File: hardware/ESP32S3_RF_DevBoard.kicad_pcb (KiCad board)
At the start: 4 copper layers, 25.4 x 60 mm, 35 parts, among them J1 USB4105-GF-A, J2 Conn_01x22, J3 Conn_01x22, SW1 BOOT, SW2 RESET, U1 ESD122DMYR, U2 LD1117DT33CTR, U3 ESP32-S3-WROOM-1-N8, U4 SN74AHCT1G125DBVR

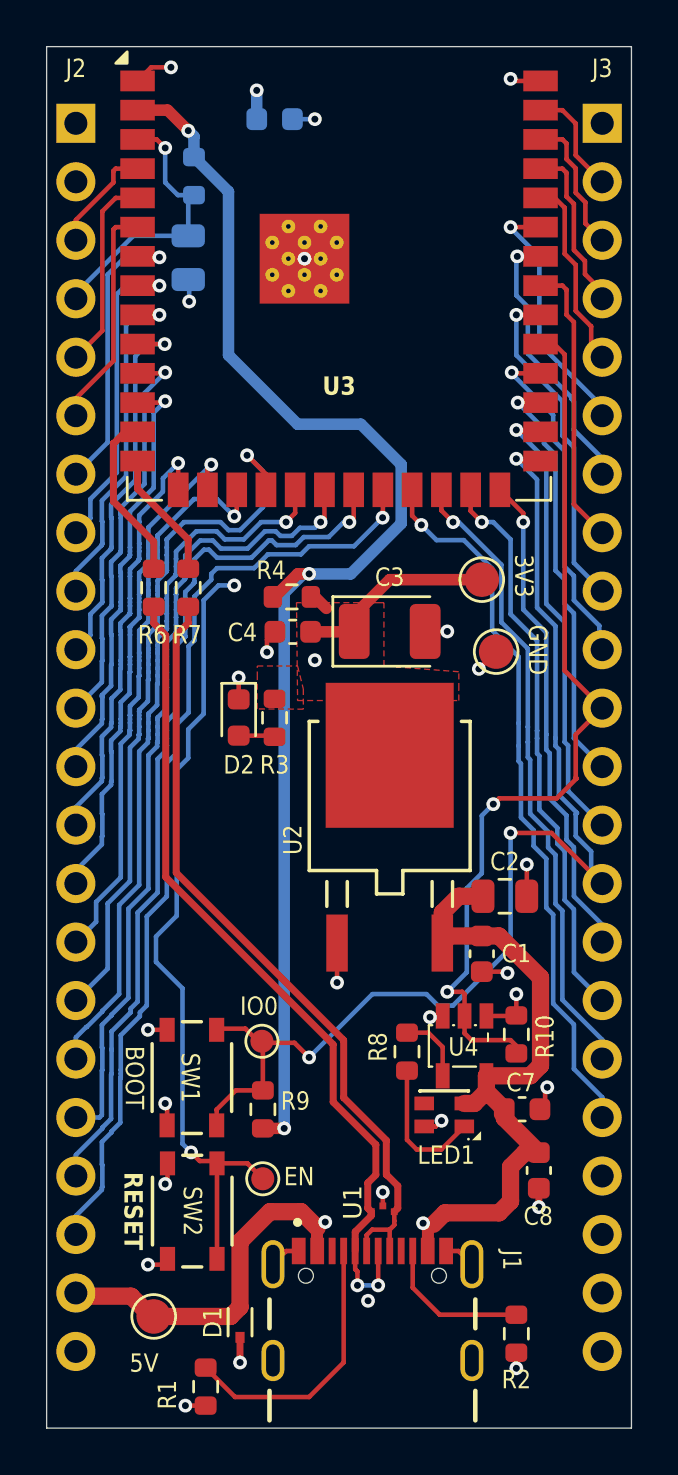
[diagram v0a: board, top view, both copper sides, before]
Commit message: - as of now i will recalculate the impedance of the board for the USB diff pairs for the JLCPCB no stackup control requiekment. - will have to change the width and gap of the USB_DIFF on the board - will have to do a minor change to the stackup and replace the 7628A dielectric structyre
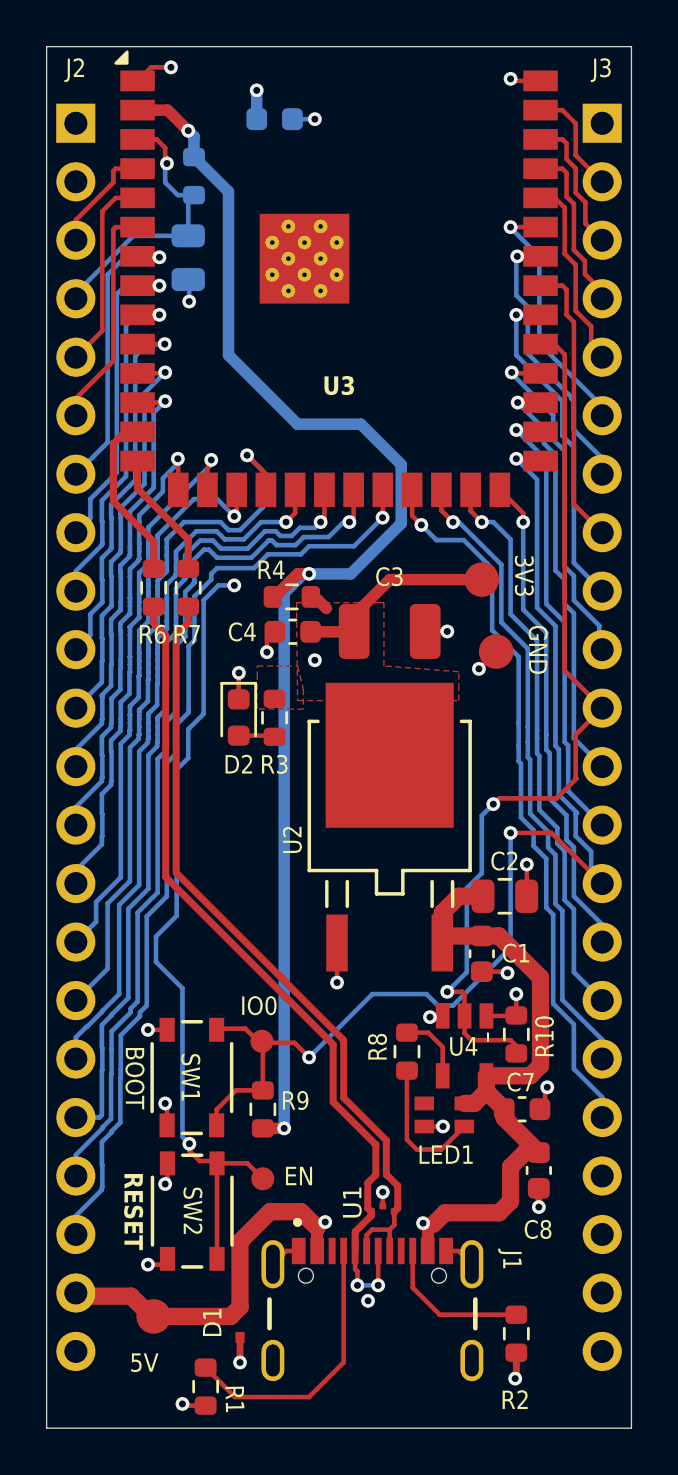
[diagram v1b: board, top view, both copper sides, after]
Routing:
- net GND: track 28.5 -> 29.3 mm, vias 26 -> 25

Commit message: - checking the drc - checking manufacturing for the USB receptacle - checking diff routing (diff imp check) rerouted - adding imgs a - adding in gerbers and drill files
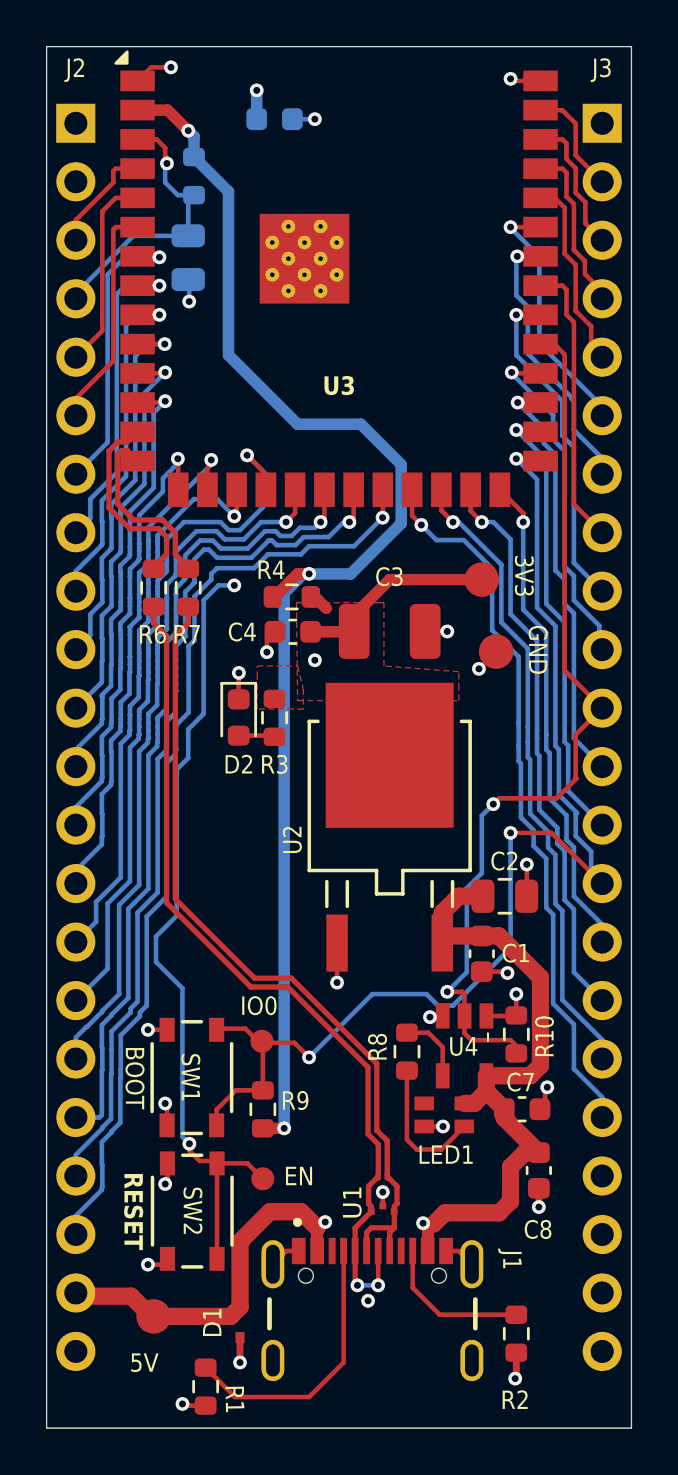
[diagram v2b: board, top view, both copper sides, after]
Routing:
- net /USB_ESP_D+: track 5.59 -> 8.06 mm
- net /USB_ESP_D-: track 7.42 -> 8.70 mm
- net /USB_D+: track 34.1 -> 35.4 mm
- net /USB_D-: track 36.4 -> 37.4 mm
